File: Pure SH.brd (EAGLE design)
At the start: 18.3 x 100 mm, 28 parts, among them T1 3904, U1 LF398, U2 4093

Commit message: SandH 1.1
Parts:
- added R7: 0R, rcl:R0805
- R2: value 10K -> 2K2***
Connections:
- net +12V: now also R7.2
- net N$3: now also R7.1
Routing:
- net N$3: track 2.93 -> 16.5 mm
- net +12V: track 77.2 -> 82.1 mm
- net GND: track 0.00 -> 2.54 mm
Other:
- board text added: "Pure S&H V1.1"
- board text removed: "Pure S&H V1.0"
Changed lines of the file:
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@@
 <?xml version="1.0" encoding="utf-8"?>
 <!DOCTYPE eagle SYSTEM "eagle.dtd">
-<eagle version="7.1.0">
+<eagle version="7.2.0">
 <drawing>
 <settings>
@@
 copyright
 GMSN Ltd 2016</text>
-<text x="17.93875" y="97.155" size="1.27" layer="22" ratio="13" rot="MR270">Pure S&amp;H V1.0</text>
-<text x="17.93875" y="82.788125" size="1.27" layer="21" ratio="13" rot="R90">Pure S&amp;H V1.0</text>
+<text x="17.93875" y="97.155" size="1.27" layer="22" ratio="13" rot="MR270">Pure S&amp;H V1.1</text>
+<text x="17.93875" y="82.788125" size="1.27" layer="21" ratio="13" rot="R90">Pure S&amp;H V1.1</text>
 <text x="18.653125" y="24.4475" size="1.27" layer="22" rot="MR270">power</text>
 <rectangle x1="4.206875" y1="16.748125" x2="6.111875" y2="26.67" layer="21"/>
@@
 <attribute name="VALUE" x="4.841875" y="77.7875" size="0.8128" layer="27" ratio="13" rot="R270"/>
 </element>
-<element name="R2" library="rcl" package="R0805" value="10K" x="14.684375" y="77.390625" smashed="yes" rot="R180">
+<element name="R2" library="rcl" package="R0805" value="2K2***" x="14.684375" y="77.390625" smashed="yes" rot="R180">
 <attribute name="NAME" x="18.335625" y="77.866875" size="0.8128" layer="25" ratio="13" rot="R180"/>
 <attribute name="VALUE" x="15.875" y="77.7875" size="0.8128" layer="27" ratio="13" rot="R180"/>
@@
 <element name="U$2" library="gmsnLogo" package="GMSN!_LOGO" value="" x="10.398125" y="113.903125"/>
 <element name="U$3" library="gmsnLogo" package="GMSN!_LOGO" value="" x="9.604375" y="113.903125" rot="MR0"/>
+<element name="R7" library="rcl" package="R0805" value="0R" x="5.000625" y="83.97875"/>
 </elements>
 <signals>
@@
 <vertex x="19.32" y="16.73"/>
 </polygon>
+<wire x1="7.62" y1="64.135" x2="5.08" y2="64.135" width="0.5" layer="1"/>
 </signal>
 <signal name="N$1">
@@
 <wire x1="11.985625" y1="51.812825" x2="14.655925" y2="51.812825" width="0.5" layer="1"/>
 <wire x1="14.655925" y1="51.812825" x2="14.875" y2="51.59375" width="0.5" layer="1"/>
-<wire x1="11.16" y1="84.25" x2="11.16" y2="84.09" width="0.5" layer="1"/>
-<wire x1="11.16" y1="84.09" x2="11.668125" y2="83.581875" width="0.5" layer="1"/>
-<wire x1="11.668125" y1="83.581875" x2="11.668125" y2="82.286975" width="0.5" layer="1"/>
-<wire x1="11.668125" y1="82.286975" x2="11.93115" y2="81.651975" width="0.5" layer="1" curve="45"/>
 <wire x1="11.93115" y1="81.651975" x2="12.22375" y2="80.945575" width="0.5" layer="1" curve="-45"/>
 <wire x1="12.22375" y1="80.945575" x2="12.22375" y2="80.1404375" width="0.5" layer="1"/>
@@
 <wire x1="16.261690625" y1="55.790440625" x2="18.018125" y2="57.546875" width="0.8" layer="1"/>
 <via x="18.018125" y="57.546875" extent="1-16" drill="0.6"/>
-<wire x1="18.018125" y1="57.546875" x2="18.494375" y2="58.023125" width="0.8" layer="16"/>
-<wire x1="18.494375" y1="58.023125" x2="18.494375" y2="66.598553125" width="0.8" layer="16"/>
+<wire x1="18.018125" y1="57.546875" x2="18.02363125" y2="57.55238125" width="0.8" layer="16"/>
+<wire x1="18.02363125" y1="57.55238125" x2="18.494375" y2="58.68885625" width="0.8" layer="16" curve="45"/>
+<wire x1="18.494375" y1="58.68885625" x2="18.494375" y2="66.598553125" width="0.8" layer="16"/>
 <wire x1="18.494375" y1="66.598553125" x2="15.746240625" y2="73.233134375" width="0.8" layer="16" curve="45"/>
 <wire x1="15.746240625" y1="73.233134375" x2="13.81125" y2="75.168125" width="0.8" layer="16"/>
@@
 <wire x1="14.875" y1="51.59375" x2="14.9225" y2="51.59375" width="0.4064" layer="1"/>
 <wire x1="14.9225" y1="51.59375" x2="14.9225" y2="51.435" width="0.4064" layer="1"/>
+<wire x1="11.93115" y1="81.651975" x2="11.16" y2="82.85" width="0.5" layer="1"/>
+<contactref element="R7" pad="2"/>
+<wire x1="5.950625" y1="83.97875" x2="6.3429875" y2="83.97875" width="0.5" layer="1"/>
+<wire x1="6.3429875" y1="83.97875" x2="7.30346875" y2="84.37659375" width="0.5" layer="1" curve="45"/>
+<wire x1="7.30346875" y1="84.37659375" x2="8.25926875" y2="84.7725" width="0.5" layer="1" curve="-45"/>
+<wire x1="8.25926875" y1="84.7725" x2="9.698721875" y2="84.7725" width="0.5" layer="1"/>
+<wire x1="9.698721875" y1="84.7725" x2="10.95375" y2="83.517471875" width="0.5" layer="1" curve="-90"/>
+<wire x1="10.95375" y1="83.517471875" x2="10.95375" y2="83.05625" width="0.5" layer="1"/>
+<wire x1="10.95375" y1="83.05625" x2="11.16" y2="82.85" width="0.5" layer="1"/>
 </signal>
 <signal name="N$4">
@@
 <contactref element="R2" pad="2"/>
 <contactref element="U$1" pad="1"/>
-<wire x1="13.734375" y1="77.390625" x2="13.532125" y2="77.390625" width="0.4" layer="1"/>
-<wire x1="13.532125" y1="77.390625" x2="12.65360625" y2="77.02673125" width="0.4" layer="1" curve="45"/>
-<wire x1="12.65360625" y1="77.02673125" x2="12.559553125" y2="76.932678125" width="0.4" layer="1"/>
-<wire x1="12.559553125" y1="76.932678125" x2="12.132109375" y2="76.755625" width="0.4" layer="1" curve="-44.999704"/>
-<wire x1="12.132109375" y1="76.755625" x2="11.665625" y2="76.755625" width="0.4" layer="1"/>
-<wire x1="11.665625" y1="76.755625" x2="11.16" y2="76.25" width="0.4" layer="1"/>
+<wire x1="13.734375" y1="77.390625" x2="11.16" y2="77.65" width="0.5" layer="1"/>
+<contactref element="R7" pad="1"/>
+<wire x1="11.16" y1="77.65" x2="11.16" y2="77.085009375" width="0.5" layer="1"/>
+<wire x1="11.16" y1="77.085009375" x2="9.798740625" y2="75.72375" width="0.5" layer="1" curve="-90"/>
+<wire x1="9.798740625" y1="75.72375" x2="8.73125" y2="75.72375" width="0.5" layer="1"/>
+<wire x1="8.73125" y1="75.72375" x2="7.540625" y2="76.914375" width="0.5" layer="1" curve="-90"/>
+<wire x1="7.540625" y1="76.914375" x2="7.540625" y2="80.07326875" width="0.5" layer="1"/>
+<wire x1="7.540625" y1="80.07326875" x2="5.38139375" y2="82.2325" width="0.5" layer="1" curve="90"/>
+<wire x1="5.38139375" y1="82.2325" x2="5.06461875" y2="82.2325" width="0.5" layer="1"/>
+<wire x1="5.06461875" y1="82.2325" x2="4.048125" y2="83.24899375" width="0.5" layer="1" curve="-90"/>
+<wire x1="4.048125" y1="83.24899375" x2="4.048125" y2="83.97625" width="0.5" layer="1"/>
+<wire x1="4.048125" y1="83.97625" x2="4.050625" y2="83.97875" width="0.5" layer="1"/>
 </signal>
 <signal name="N$14">

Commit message: SandH 1.2
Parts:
- removed R7: 0R, rcl:R0805
- removed U$1: LED_RG_SMD_REV, INSTRUO:LSG_T77K
- added C10, C8: 0.1u, rcl:C0805K
- added IC1: TL072D, linear:SO08
- added R10: 100K, rcl:R0805
- added R8, R9: 100k, rcl:R0805
- RATE: value (none) -> Q-POT
- moved R3 27.5 mm to (2.62, 87.0), turned to 270 degrees
- moved C2 21.8 mm to (8.65, 65.7), turned to 180 degrees
- moved U1 21.8 mm to (10.3, 71.2)
- moved C3 21.5 mm to (4.37, 73.3)
- moved C9 21.0 mm to (14.8, 72.5), turned to 270 degrees
- moved U2 19.7 mm to (9.37, 87.6), turned to 270 degrees
- moved C1 19.1 mm to (5.64, 82.9), turned to 180 degrees
- moved C6 17.0 mm to (17.7, 89.2), turned to 90 degrees
- moved T1 11.5 mm to (16.1, 84.5)
- moved R2 11.3 mm to (15.3, 88.7), turned to 90 degrees
- moved R4 11.3 mm to (15.6, 68.8), turned to 180 degrees
- moved R5 8.58 mm to (16.7, 55.4), turned to 90 degrees
- moved R6 8.44 mm to (4.05, 94.5)
- moved D1 6.95 mm to (16.3, 76.5)
- moved C7 6.61 mm to (9.92, 96.4), turned to 0 degrees
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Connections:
- removed net N$3: R2.2, R7.1, U$1.1
- new net N$12: IC1.2, R5.1, R8.2
- new net N$16: IC1.1, R8.1, U1.3
- new net N$17: R10.2, U1.5
- new net N$18: IC1.6, R10.1, R9.2
- new net N$19: IC1.7, OUT.TIP, R9.1
- new net N$21: C8.1, IC1.8
- net +12V: now also R2.2; no longer R7.2, U$1.2
- net GND: now also C10.1, C8.2, IC1.3, IC1.5; no longer R5.1
- net N$11: no longer U1.3
- net N$20: now also C10.2, IC1.4; no longer OUT.TIP, U1.5
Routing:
- net N$16: track 0.00 -> 39.6 mm, vias 0 -> 2
- net N$14: track 49.0 -> 11.6 mm, vias 1 -> 0
- net N$6: track 30.8 -> 2.47 mm, vias 2 -> 0
- net N$9: track 3.27 -> 30.6 mm, vias 0 -> 2
- net -12V: track 29.7 -> 56.4 mm
- net N$18: track 0.00 -> 21.8 mm
- net N$3: track 16.5 -> 0.00 mm
- net N$19: track 0.00 -> 13.8 mm
- net N$12: track 0.00 -> 7.27 mm
- net N$20: track 7.87 -> 3.30 mm
- net N$17: track 0.00 -> 4.54 mm
- net N$2: track 20.3 -> 15.9 mm, vias 2 -> 0
- net N$11: track 10.1 -> 13.6 mm
- net +12V: track 82.1 -> 85.3 mm, vias 3 -> 0
- net N$21: track 0.00 -> 3.01 mm
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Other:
- board text added: "Pure S&H V1.2"
- board text added: "copyright GMSN Ltd 2016"
- board text removed: "Designed by Jason H. J. Lim and Rob Spencer copyright GMSN Ltd 2016"
- board text removed: "Pure S&H V1.1"

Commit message: SandH 1.3
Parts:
- removed U2: 4093, QuBit:SOIC14
- added IC2: 4093D, 40xx:SO14
- moved C1 30.5 mm to (11.3, 112.9), turned to 0 degrees
- moved C6 25.9 mm to (3.57, 111.0)
- moved R3 25.9 mm to (16.1, 109.1), turned to 90 degrees
- moved U$2 13.6 mm to (2.70, 102.7), turned to 90 degrees
- moved D1 10.4 mm to (9.68, 84.6)
- moved R1 9.26 mm to (5.16, 85.8), turned to 90 degrees
- moved T1 7.77 mm to (9.53, 88.6), turned to 0 degrees
- moved C8 4.19 mm to (6.43, 44.6), turned to 270 degrees
- moved C7 3.65 mm to (13.6, 96.4)
- moved C10 2.45 mm to (12.5, 54.5), turned to 270 degrees
- moved R8 2.18 mm to (16.3, 48.5)
- moved R10 2.17 mm to (5.00, 67.7)
- moved R9 1.75 mm to (3.81, 49.5)
- moved C9 1.75 mm to (14.8, 74.3), turned to 90 degrees
- moved R2 1.67 mm to (13.7, 88.7), turned to 270 degrees
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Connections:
- removed net N$20: C10.2, IC1.4
- removed net N$21: C8.1, IC1.8
- net +12V: now also C8.1, IC1.8, IC2.14; no longer U2.14
- net -12V: now also C10.2, IC1.4
- net GND: now also IC2.7
- net N$14: now also IC2.5, IC2.6; no longer U2.5, U2.6
- net N$15: now also IC2.4; no longer U2.4
- net N$4: now also IC2.12, IC2.13; no longer U2.12, U2.13
- net N$5: now also IC2.11; no longer U2.11
- net N$7: now also IC2.8, IC2.9; no longer U2.8, U2.9
- net N$8: now also IC2.1, IC2.10, IC2.2; no longer U2.1, U2.10, U2.2
- net N$9: now also IC2.3; no longer U2.3
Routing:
- net +12V: track 85.3 -> 138.4 mm
- net N$4: track 9.48 -> 38.7 mm, vias 0 -> 2
- net N$15: track 27.2 -> 44.1 mm, vias 1 -> 0
- net N$9: track 30.6 -> 44.6 mm
- net N$2: track 15.9 -> 6.60 mm
- net -12V: track 56.4 -> 64.4 mm, vias 0 -> 2
- net N$20: track 3.30 -> 0.00 mm
- net N$21: track 3.01 -> 0.00 mm
- net N$14: track 11.6 -> 14.5 mm
- net N$7: track 8.67 -> 6.58 mm
- net N$13: track 4.85 -> 3.14 mm
- net N$5: track 4.63 -> 2.96 mm
- net N$16: track 39.6 -> 38.2 mm
- net N$19: track 13.8 -> 12.6 mm
- net N$17: track 4.54 -> 3.49 mm
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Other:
- board text added: "Pure S&H V1.3"
- board text removed: "Pure S&H V1.2"

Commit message: SandH 1.4
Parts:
- removed U1: LF398, QuBit:SOIC--8
- added C11: 100nF, GMSN:C0805
- added IC3: cd4093, GMSN:SOIC14
- added R7: 1k, GMSN:R0805
- C1, C7: device rcl:C0805K -> GMSN:C0805
- C10, C3, C6, C8, C9: value 0.1u -> 100nF; device rcl:C0805K -> GMSN:C0805
- C2: value 0.1u -> Polypropylene Film 4.7nF; device rcl:C0805K -> GMSN:C050-045X075
- C4, C5: value 10u -> 10uF; device rcl:153CLV-0505 -> GMSN:153CLV-0505
- CLK, IN, OUT: value (none) -> PJ301M-12; device INSTRUO:S_JACK -> GMSN:PJ301M-12
- D1: device SparkFun-DiscreteSemi:SOD-323 -> GMSN:DO-41
- D2, D3: value (none) -> STTH102A; device adafruit:SMADIODE -> GMSN:DO-41
- IC1: value TL072D -> LF398; device linear:SO08 -> GMSN:SOIC--8
- IC2: value 4093D -> TL072; device 40xx:SO14 -> GMSN:SO08
- PWR: value (none) -> HEADER2X5SHD; device SparkFun-Connectors:2X5-SHROUDED -> GMSN:2X5-SHROUDED
- R1, R10, R5: value 100K -> 100k; device rcl:R0805 -> GMSN:R0805
- R2: value 2K2*** -> 2K2; device rcl:R0805 -> GMSN:R0805
- R3: value 10K -> 10k; device rcl:R0805 -> GMSN:R0805
- R4: value 1K -> 5k6; device rcl:R0805 -> GMSN:R0805
- R6: value 2K2 -> 2k2; device rcl:R0805 -> GMSN:R0805
- R8, R9: device rcl:R0805 -> GMSN:R0805
- RATE: device QuBit:Q-POT -> GMSN:POTENTIOMETER_9MM
- T1: value 3904 -> MMBT3904; device QuBit:TRANSISTOR_SINGLE_N-TYPE -> GMSN:SOT23
- moved IC2 57.4 mm to (10.2, 49.5), turned to 90 degrees
- moved IC1 17.9 mm to (10.2, 67.3)
- moved C3 13.8 mm to (15.2, 63.5), turned to 180 degrees
- moved C9 12.7 mm to (5.08, 66.0), turned to 180 degrees
- moved R4 12.3 mm to (3.81, 73.7), turned to 270 degrees
- moved R10 10.3 mm to (15.2, 68.6)
- moved C2 9.30 mm to (12.9, 74.0), turned to 0 degrees
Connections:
- removed net N$8: IC2.1, IC2.10, IC2.2
- new net N$3: C1.1, IC3.11
- net +12V: now also C11.1, IC1.1, IC2.8, IC3.14; no longer IC1.8, IC2.14, U1.1
- net -12V: now also IC2.4; no longer U1.4
- net GND: now also C11.2, D1.A, IC1.7, IC2.3, IC2.5, IC3.7, R7.1, T1.2; no longer D1.2, IC1.3, IC1.5, IC2.7, T1.E, U1.7
- net N$10: now also IC1.6; no longer U1.6
- net N$12: now also IC2.2; no longer IC1.2
- net N$14: now also IC3.5, IC3.6; no longer IC2.5, IC2.6
- net N$15: now also IC3.4; no longer IC2.4
- net N$16: now also IC1.3, IC2.1; no longer IC1.1, U1.3
- net N$17: now also IC1.5; no longer U1.5
- net N$18: now also IC2.6; no longer IC1.6
- net N$19: now also IC2.7; no longer IC1.7
- net N$2: now also D1.C, T1.1; no longer D1.1, T1.B
- net N$4: now also IC3.12, IC3.13, T1.3; no longer IC2.12, IC2.13, T1.C
- net N$5: now also IC3.1, IC3.10, IC3.2; no longer C1.1, IC2.11
- net N$6: now also IC1.8, R7.2; no longer U1.8
- net N$7: now also IC3.8, IC3.9; no longer IC2.8, IC2.9
- net N$9: now also IC3.3; no longer IC2.3
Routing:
- net +12V: track 138.4 -> 150.5 mm
- net N$8: track 9.97 -> 0.00 mm
- net N$16: track 38.2 -> 31.3 mm, vias 2 -> 0
- net N$18: track 21.2 -> 27.1 mm, vias 0 -> 2
- net N$6: track 1.99 -> 7.77 mm
- net N$5: track 2.96 -> 7.91 mm
- net N$2: track 6.60 -> 11.5 mm
- net N$3: track 0.00 -> 3.69 mm
- net N$50: track 8.98 -> 12.2 mm
- net N$38: track 8.91 -> 12.1 mm
- net -12V: track 64.4 -> 66.6 mm
- net N$4: track 38.7 -> 40.1 mm
- net N$9: track 44.6 -> 43.5 mm
- net N$10: track 3.63 -> 4.47 mm
- net N$12: track 7.83 -> 8.61 mm
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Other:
- board text added: "Pure S&H V1.4"
- board text added: "cc-by 4.0"
- board text removed: "Pure S&H V1.3"
- board text removed: "copyright GMSN Ltd 2016"

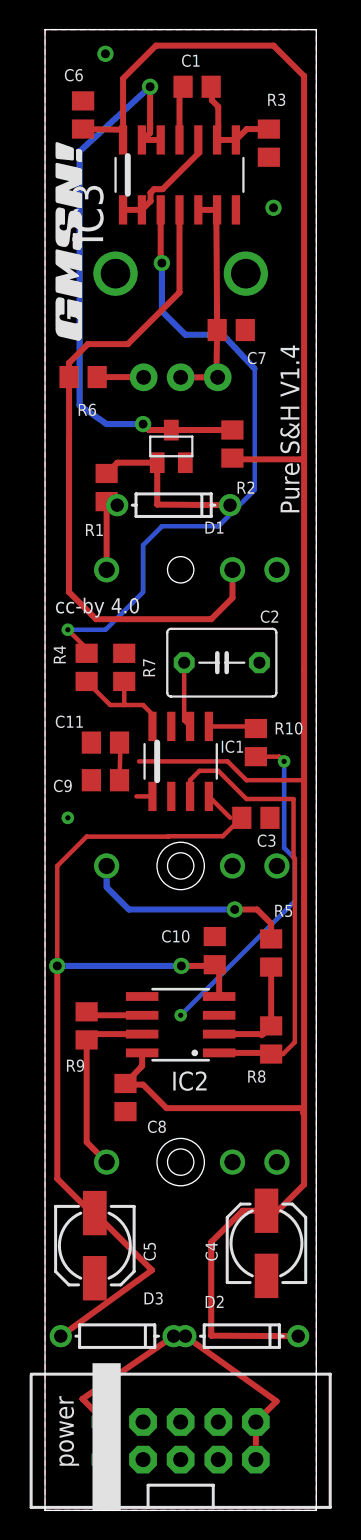
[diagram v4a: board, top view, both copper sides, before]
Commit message: SandH 1.5
S&H Updated to V1.5 14/4/21

Library updated to include 3D models.
Traces rerouted.
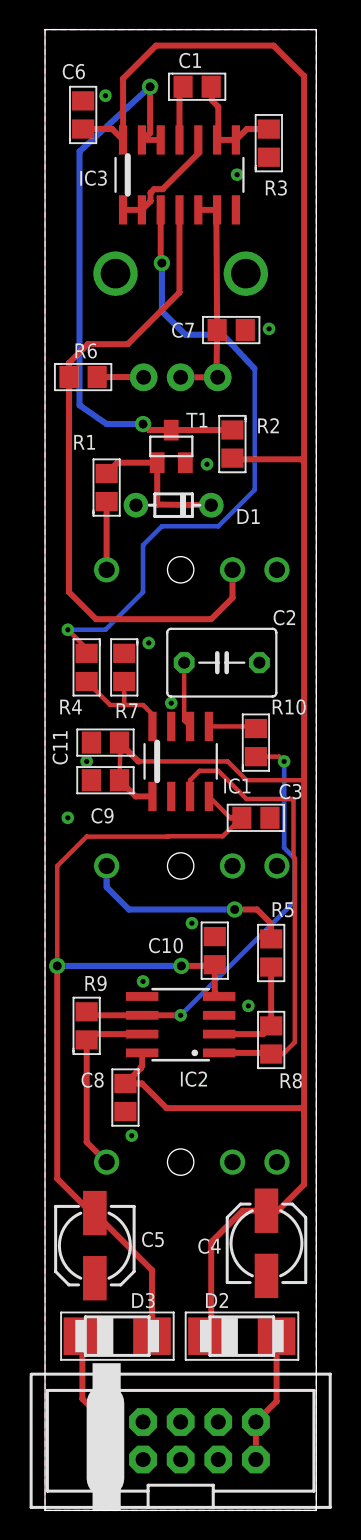
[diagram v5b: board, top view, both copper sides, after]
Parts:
- removed U$2: (no value), gmsnLogo:GMSN!_LOGO
- D2, D3: device GMSN:DO-41 -> GMSN:SMADIODE
- moved U$3 25.4 mm to (9.68, 89.6)
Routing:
- net N$50: track 12.2 -> 8.98 mm
- net N$38: track 12.1 -> 8.91 mm
- net -12V: track 66.6 -> 64.1 mm
- net N$18: track 27.1 -> 29.1 mm
- net N$2: track 11.5 -> 10.2 mm
- net +12V: track 150.5 -> 149.5 mm
- net N$12: track 8.61 -> 7.71 mm
- net N$14: track 14.4 -> 15.1 mm
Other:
- board text added: "Pure S&H V1.5 cc-by 4.0 2021 The Little Red Hen"
- board text removed: "Pure S&H V1.4"
- board text removed: "cc-by 4.0"
- board text removed: "power"

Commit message: Reinstall
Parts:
- R10, R5, R8, R9: value 100k -> 10k
- R2: value 2K2 -> 2k2
- RATE: value Q-POT -> A1M
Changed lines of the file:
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@@
 <drawing>
 <settings>
-<setting alwaysvectorfont="yes"/>
+<setting alwaysvectorfont="no"/>
 <setting keepoldvectorfont="yes"/>
 <setting verticaltext="up"/>
@@
 <attribute name="SORT" value="2" x="5.159375" y="85.804375" size="1.778" layer="27" rot="R90" display="off"/>
 </element>
-<element name="R2" library="GMSN" library_urn="urn:adsk.eagle:library:27425118" package="R0805" package3d_urn="urn:adsk.eagle:package:27425978/1" value="2K2" x="13.6525" y="88.74125" smashed="yes" rot="R270">
+<element name="R2" library="GMSN" library_urn="urn:adsk.eagle:library:27425118" package="R0805" package3d_urn="urn:adsk.eagle:package:27425978/1" value="2k2" x="13.6525" y="88.74125" smashed="yes" rot="R270">
 <attribute name="NAME" x="15.27175" y="89.4715" size="1" layer="25"/>
 <attribute name="SORT" value="2" x="13.6525" y="88.74125" size="1.778" layer="27" rot="R270" display="off"/>
@@
 <attribute name="SORT" value="2" x="3.81" y="73.66" size="1.778" layer="27" rot="R270" display="off"/>
 </element>
-<element name="R5" library="GMSN" library_urn="urn:adsk.eagle:library:27425118" package="R0805" package3d_urn="urn:adsk.eagle:package:27425978/1" value="100k" x="16.271875" y="54.371875" smashed="yes" rot="R90">
+<element name="R5" library="GMSN" library_urn="urn:adsk.eagle:library:27425118" package="R0805" package3d_urn="urn:adsk.eagle:package:27425978/1" value="10k" x="16.271875" y="54.371875" smashed="yes" rot="R90">
 <attribute name="NAME" x="17.891125" y="57.800875" size="1" layer="25" rot="R180"/>
 <attribute name="SORT" value="2" x="16.271875" y="54.371875" size="1.778" layer="27" rot="R90" display="off"/>
@@
 <attribute name="SORT" value="2" x="3.571875" y="93.265625" size="1.778" layer="27" display="off"/>
 </element>
-<element name="RATE" library="GMSN" library_urn="urn:adsk.eagle:library:27425118" package="POTENTIOMETER_9MM" package3d_urn="urn:adsk.eagle:package:27425927/2" value="Q-POT" x="10.16" y="100.25" smashed="yes" rot="MR0">
+<element name="RATE" library="GMSN" library_urn="urn:adsk.eagle:library:27425118" package="POTENTIOMETER_9MM" package3d_urn="urn:adsk.eagle:package:27425927/2" value="A1M" x="10.16" y="100.25" smashed="yes" rot="MR0">
 <attribute name="SORT" value="8" x="10.16" y="100.25" size="1.778" layer="28" rot="MR0" display="off"/>
 </element>
@@
 </element>
 <element name="U$3" library="gmsnLogo" package="GMSN!_LOGO" value="" x="9.68375" y="89.614375" smashed="yes" rot="MR0"/>
-<element name="R8" library="GMSN" library_urn="urn:adsk.eagle:library:27425118" package="R0805" package3d_urn="urn:adsk.eagle:package:27425978/1" value="100k" x="16.271875" y="48.498125" smashed="yes" rot="R90">
+<element name="R8" library="GMSN" library_urn="urn:adsk.eagle:library:27425118" package="R0805" package3d_urn="urn:adsk.eagle:package:27425978/1" value="10k" x="16.271875" y="48.498125" smashed="yes" rot="R90">
 <attribute name="NAME" x="18.430875" y="46.243875" size="1" layer="25" rot="R180"/>
 <attribute name="SORT" value="2" x="16.271875" y="48.498125" size="1.778" layer="27" rot="R90" display="off"/>
 </element>
-<element name="R9" library="GMSN" library_urn="urn:adsk.eagle:library:27425118" package="R0805" package3d_urn="urn:adsk.eagle:package:27425978/1" value="100k" x="3.81" y="49.450625" smashed="yes" rot="R90">
+<element name="R9" library="GMSN" library_urn="urn:adsk.eagle:library:27425118" package="R0805" package3d_urn="urn:adsk.eagle:package:27425978/1" value="10k" x="3.81" y="49.450625" smashed="yes" rot="R90">
 <attribute name="NAME" x="3.603625" y="51.816" size="1" layer="25"/>
 <attribute name="SORT" value="2" x="3.81" y="49.450625" size="1.778" layer="27" rot="R90" display="off"/>
 </element>
-<element name="R10" library="GMSN" library_urn="urn:adsk.eagle:library:27425118" package="R0805" package3d_urn="urn:adsk.eagle:package:27425978/1" value="100k" x="15.24" y="68.58" smashed="yes" rot="R90">
+<element name="R10" library="GMSN" library_urn="urn:adsk.eagle:library:27425118" package="R0805" package3d_urn="urn:adsk.eagle:package:27425978/1" value="10k" x="15.24" y="68.58" smashed="yes" rot="R90">
 <attribute name="NAME" x="16.256" y="70.485" size="1" layer="25"/>
 <attribute name="SORT" value="2" x="15.24" y="68.58" size="1.778" layer="27" rot="R90" display="off"/>
